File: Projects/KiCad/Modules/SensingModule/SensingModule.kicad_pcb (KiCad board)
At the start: 2 copper layers, 110 x 95 mm, 45 parts, among them J1 Conn_01x08, J2 Conn_01x02_Pin, J4 Micro_SD_Card_Det_Hirose_DM3AT, SW1 SW_DIP_x02, U1 MCP2562-E-P, U4 TLP222A, U5 NUCLEO-F303K8, U6 MB85RS2MT, U7 MB85RS2MT

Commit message: チェックよし（多分）
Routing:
- net MEMORY_POWER: track 60.9 -> 61.8 mm
- net GND: vias 170 -> 169
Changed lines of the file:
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@@
     (fp_line (start 1 0.625) (end -1 0.625)
       (stroke (width 0.1) (type solid)) (layer "F.Fab"))
-    (pad "1" smd roundrect (at -1 0) (size 1.2 1.4) (layers "F.Cu" "F.Paste" "F.Mask") (roundrect_rratio 0.208333)
+    (pad "1" smd roundrect (at -1 0) (size 1.2 1.4) (layers "F.Cu" "F.Paste" "F.Mask") (roundrect_rratio 0.2083333333)
       (net 35 "CAN_RECEIVE_STATUS") (pintype "passive"))
-    (pad "2" smd roundrect (at 1 0) (size 1.2 1.4) (layers "F.Cu" "F.Paste" "F.Mask") (roundrect_rratio 0.208333)
+    (pad "2" smd roundrect (at 1 0) (size 1.2 1.4) (layers "F.Cu" "F.Paste" "F.Mask") (roundrect_rratio 0.2083333333)
       (net 15 "Net-(D1-A)") (pintype "passive"))
     (model "${KICAD6_3DMODEL_DIR}/Resistor_SMD.3dshapes/R_0805_2012Metric.wrl"
@@
     (fp_line (start 1 0.625) (end -1 0.625)
       (stroke (width 0.1) (type solid)) (layer "F.Fab"))
-    (pad "1" smd roundrect (at -1 0) (size 1.2 1.4) (layers "F.Cu" "F.Paste" "F.Mask") (roundrect_rratio 0.208333)
+    (pad "1" smd roundrect (at -1 0) (size 1.2 1.4) (layers "F.Cu" "F.Paste" "F.Mask") (roundrect_rratio 0.2083333333)
       (net 34 "CAN_SEND_STATUS") (pintype "passive"))
-    (pad "2" smd roundrect (at 1 0) (size 1.2 1.4) (layers "F.Cu" "F.Paste" "F.Mask") (roundrect_rratio 0.208333)
+    (pad "2" smd roundrect (at 1 0) (size 1.2 1.4) (layers "F.Cu" "F.Paste" "F.Mask") (roundrect_rratio 0.2083333333)
       (net 10 "Net-(D2-A)") (pintype "passive"))
     (model "${KICAD6_3DMODEL_DIR}/Resistor_SMD.3dshapes/R_0805_2012Metric.wrl"
@@
     (fp_line (start 1 0.625) (end -1 0.625)
       (stroke (width 0.1) (type solid)) (layer "F.Fab"))
-    (pad "1" smd roundrect (at -1 0 90) (size 1.2 1.4) (layers "F.Cu" "F.Paste" "F.Mask") (roundrect_rratio 0.208333)
+    (pad "1" smd roundrect (at -1 0 90) (size 1.2 1.4) (layers "F.Cu" "F.Paste" "F.Mask") (roundrect_rratio 0.2083333333)
       (net 4 "+3.3V") (pintype "passive"))
-    (pad "2" smd roundrect (at 1 0 90) (size 1.2 1.4) (layers "F.Cu" "F.Paste" "F.Mask") (roundrect_rratio 0.208333)
+    (pad "2" smd roundrect (at 1 0 90) (size 1.2 1.4) (layers "F.Cu" "F.Paste" "F.Mask") (roundrect_rratio 0.2083333333)
       (net 18 "THERMISTOR") (pintype "passive"))
     (model "${KICAD6_3DMODEL_DIR}/Resistor_SMD.3dshapes/R_0805_2012Metric.wrl"
@@
     (fp_line (start 1 0.625) (end -1 0.625)
       (stroke (width 0.1) (type solid)) (layer "F.Fab"))
-    (pad "1" smd roundrect (at -1 0 90) (size 1.2 1.4) (layers "F.Cu" "F.Paste" "F.Mask") (roundrect_rratio 0.208333)
+    (pad "1" smd roundrect (at -1 0 90) (size 1.2 1.4) (layers "F.Cu" "F.Paste" "F.Mask") (roundrect_rratio 0.2083333333)
       (net 4 "+3.3V") (pintype "passive"))
-    (pad "2" smd roundrect (at 1 0 90) (size 1.2 1.4) (layers "F.Cu" "F.Paste" "F.Mask") (roundrect_rratio 0.208333)
+    (pad "2" smd roundrect (at 1 0 90) (size 1.2 1.4) (layers "F.Cu" "F.Paste" "F.Mask") (roundrect_rratio 0.2083333333)
       (net 29 "I2C_SDA") (pintype "passive"))
     (model "${KICAD6_3DMODEL_DIR}/Resistor_SMD.3dshapes/R_0805_2012Metric.wrl"
@@
     (fp_line (start 1 0.625) (end -1 0.625)
       (stroke (width 0.1) (type solid)) (layer "F.Fab"))
-    (pad "1" smd roundrect (at -1 0 90) (size 1.2 1.4) (layers "F.Cu" "F.Paste" "F.Mask") (roundrect_rratio 0.208333)
+    (pad "1" smd roundrect (at -1 0 90) (size 1.2 1.4) (layers "F.Cu" "F.Paste" "F.Mask") (roundrect_rratio 0.2083333333)
       (net 4 "+3.3V") (pintype "passive"))
-    (pad "2" smd roundrect (at 1 0 90) (size 1.2 1.4) (layers "F.Cu" "F.Paste" "F.Mask") (roundrect_rratio 0.208333)
+    (pad "2" smd roundrect (at 1 0 90) (size 1.2 1.4) (layers "F.Cu" "F.Paste" "F.Mask") (roundrect_rratio 0.2083333333)
       (net 30 "I2C_SCL") (pintype "passive"))
     (model "${KICAD6_3DMODEL_DIR}/Resistor_SMD.3dshapes/R_0805_2012Metric.wrl"
@@
     (effects (font (size 1 1) (thickness 0.153)) (justify left))
   )
-  (gr_text "CAN-BUS\nTermination Resistor" (at 187.5 124.949432) (layer "F.SilkS")
+  (gr_text "CAN-BUS\nTermination Resistor" (at 188.5812 125.066232) (layer "F.SilkS")
     (effects (font (size 1 1) (thickness 0.153)))
   )
@@
   (via (at 164.4 143.2) (size 0.51) (drill 0.25) (layers "F.Cu" "B.Cu") (free) (net 2))
   (via (at 170.6 116.4) (size 0.51) (drill 0.25) (layers "F.Cu" "B.Cu") (free) (net 2))
-  (via (at 170.4 124.2) (size 0.51) (drill 0.25) (layers "F.Cu" "B.Cu") (free) (net 2))
   (via (at 165.772 128.063432) (size 0.51) (drill 0.25) (layers "F.Cu" "B.Cu") (free) (net 2))
   (via (at 156.2 107.8) (size 0.51) (drill 0.25) (layers "F.Cu" "B.Cu") (free) (net 2))
@@
   (segment (start 146.825 108.675) (end 150 108.675) (width 0.3) (layer "F.Cu") (net 18))
   (via (at 146.825 108.675) (size 0.51) (drill 0.25) (layers "F.Cu" "B.Cu") (net 18))
-  (segment (start 131 126.5) (end 129.704 127.796) (width 0.3) (layer "B.Cu") (net 18))
+  (segment (start 145.5 110) (end 145.5 125.5) (width 0.3) (layer "B.Cu") (net 18))
+  (segment (start 129.704 132.624) (end 129.77 132.69) (width 0.3) (layer "B.Cu") (net 18))
   (segment (start 146.825 108.675) (end 145.5 110) (width 0.3) (layer "B.Cu") (net 18))
-  (segment (start 144.5 126.5) (end 131 126.5) (width 0.3) (layer "B.Cu") (net 18))
   (segment (start 129.704 127.796) (end 129.704 132.624) (width 0.3) (layer "B.Cu") (net 18))
-  (segment (start 129.704 132.624) (end 129.77 132.69) (width 0.3) (layer "B.Cu") (net 18))
-  (segment (start 145.5 110) (end 145.5 125.5) (width 0.3) (layer "B.Cu") (net 18))
+  (segment (start 131 126.5) (end 129.704 127.796) (width 0.3) (layer "B.Cu") (net 18))
+  (segment (start 144.5 126.5) (end 131 126.5) (width 0.3) (layer "B.Cu") (net 18))
   (segment (start 145.5 125.5) (end 144.5 126.5) (width 0.3) (layer "B.Cu") (net 18))
   (segment (start 123 92) (end 123 90.7) (width 0.2) (layer "F.Cu") (net 19))
@@
   (via (at 147 110.5) (size 0.51) (drill 0.25) (layers "F.Cu" "B.Cu") (net 27))
   (segment (start 147 112.5) (end 147 110.5) (width 0.3) (layer "B.Cu") (net 27))
-  (segment (start 138.955 118) (end 127 118) (width 0.5) (layer "F.Cu") (net 28))
   (segment (start 115.13 116.38) (end 113.5 114.75) (width 0.5) (layer "F.Cu") (net 28))
   (segment (start 116.62 103.88) (end 117.5 103) (width 0.5) (layer "F.Cu") (net 28))
+  (segment (start 138.955 118) (end 134.6824 118) (width 0.5) (layer "F.Cu") (net 28))
   (segment (start 117.5 92) (end 118.7 90.8) (width 0.5) (layer "F.Cu") (net 28))
+  (segment (start 134.6824 118) (end 127 118) (width 0.5) (layer "F.Cu") (net 28))
+  (segment (start 134.7 118.0176) (end 134.6824 118) (width 0.5) (layer "F.Cu") (net 28))
   (segment (start 127 118) (end 123.6 118) (width 0.5) (layer "F.Cu") (net 28))
   (segment (start 115.12 103.88) (end 116.62 103.88) (width 0.5) (layer "F.Cu") (net 28))
   (segment (start 117.5 103) (end 117.5 92) (width 0.5) (layer "F.Cu") (net 28))
+  (segment (start 134.7 118.949432) (end 134.7 118.0176) (width 0.5) (layer "F.Cu") (net 28))
   (segment (start 116.62 116.38) (end 115.13 116.38) (width 0.5) (layer "F.Cu") (net 28))
   (segment (start 113.5 105.5) (end 115.12 103.88) (width 0.5) (layer "F.Cu") (net 28))

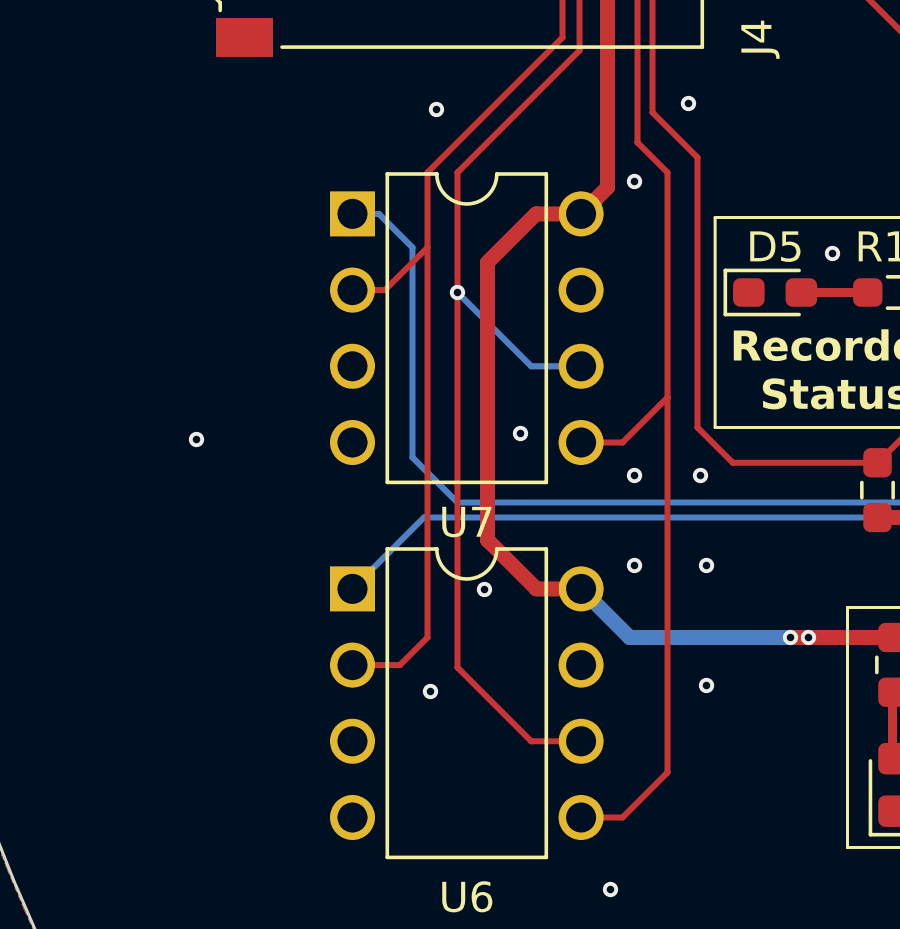
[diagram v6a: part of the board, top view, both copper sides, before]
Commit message: FRAMのWPとHOLDをHIGHに固定
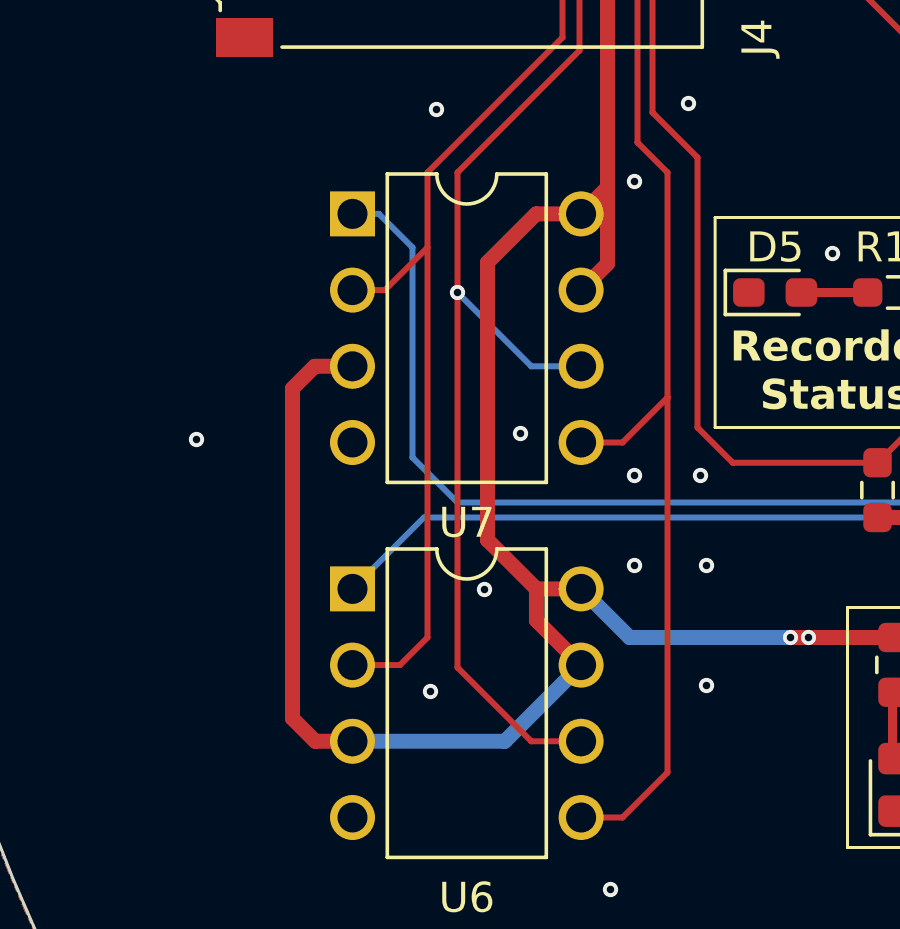
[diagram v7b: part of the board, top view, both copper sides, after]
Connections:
- U6 pad 3: GND -> MEMORY_POWER
- U6 pad 7: GND -> MEMORY_POWER
- U7 pad 3: GND -> MEMORY_POWER
- U7 pad 7: GND -> MEMORY_POWER
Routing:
- net MEMORY_POWER: track 61.8 -> 93.1 mm

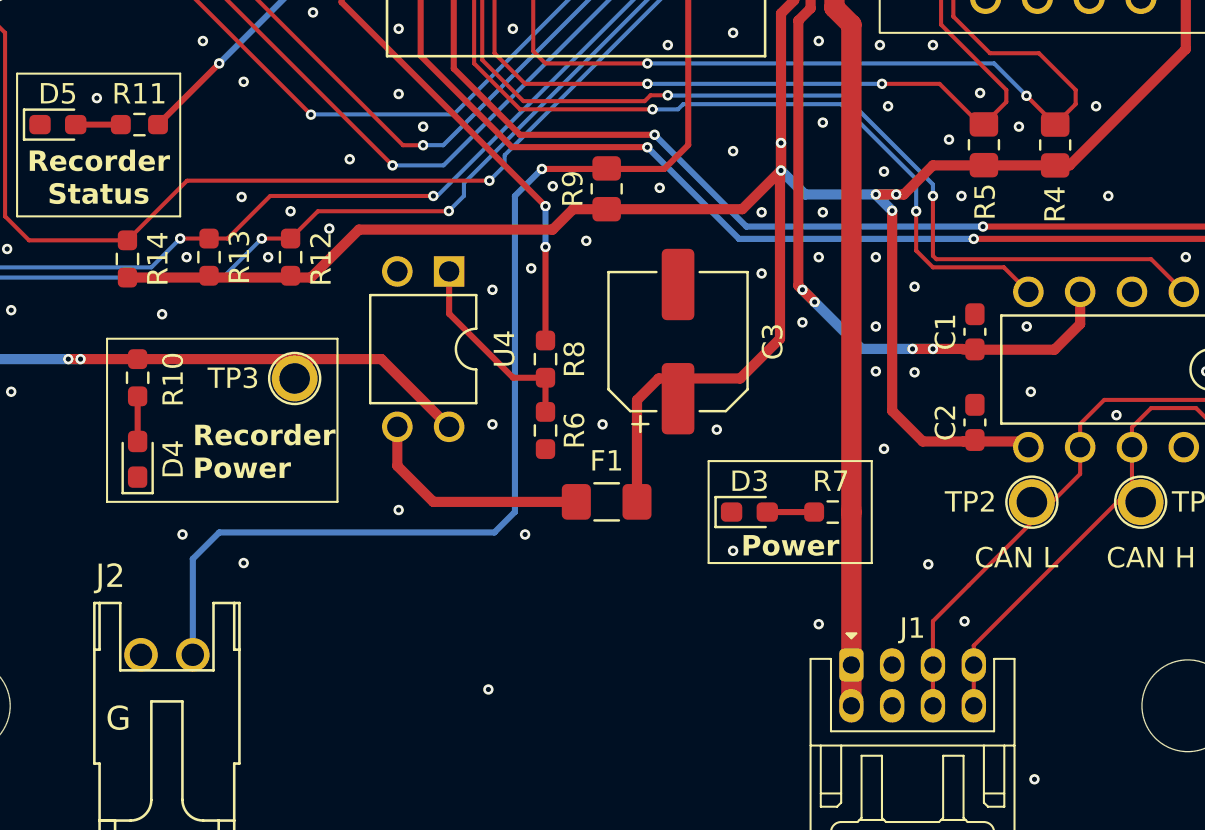
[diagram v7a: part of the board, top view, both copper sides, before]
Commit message: 計測モジュールの回路図を分割
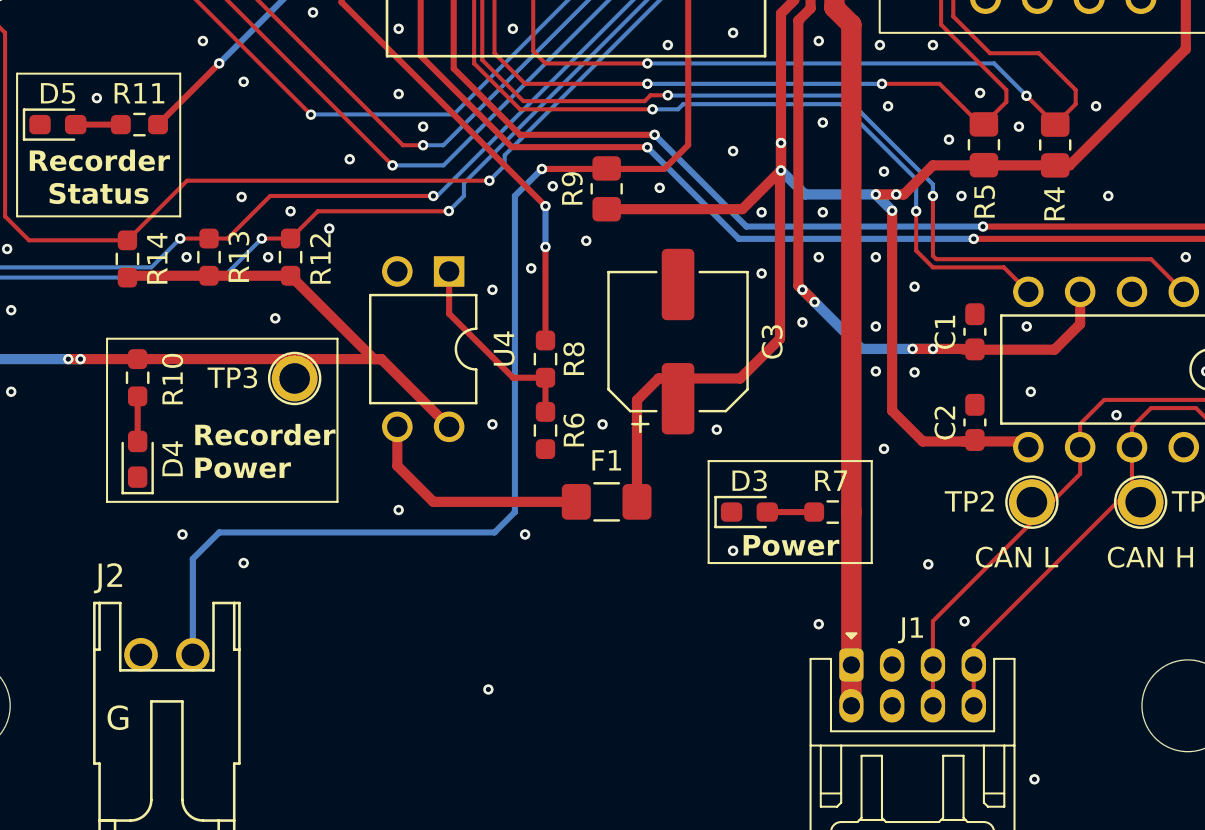
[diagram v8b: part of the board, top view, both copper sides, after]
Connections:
- net MEMORY_POWER_CONTROL renamed RECORDER_POWER_CONTROL
- J4 pad 4: MEMORY_POWER -> RECORDER_POWER
- R10 pad 1: MEMORY_POWER -> RECORDER_POWER
- R12 pad 1: +3.3V -> RECORDER_POWER
- R13 pad 1: +3.3V -> RECORDER_POWER
- R14 pad 1: +3.3V -> RECORDER_POWER
- TP3 pad 1: MEMORY_POWER -> RECORDER_POWER
- U4 pad 4: MEMORY_POWER -> RECORDER_POWER
- U6 pad 3: MEMORY_POWER -> RECORDER_POWER
- U6 pad 7: MEMORY_POWER -> RECORDER_POWER
- U6 pad 8: MEMORY_POWER -> RECORDER_POWER
- U7 pad 3: MEMORY_POWER -> RECORDER_POWER
- U7 pad 7: MEMORY_POWER -> RECORDER_POWER
- U7 pad 8: MEMORY_POWER -> RECORDER_POWER
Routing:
- net RECORDER_POWER: track 0.00 -> 107.1 mm, vias 0 -> 2
- net MEMORY_POWER: track 93.1 -> 0.00 mm, vias 2 -> 0
- net +3.3V: track 146.7 -> 121.8 mm
